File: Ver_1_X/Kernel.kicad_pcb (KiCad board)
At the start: 2 copper layers, 48.3 x 26.7 mm, 19 parts, among them J1 USB_C_Receptacle_USB2.0, J2 L, J3 R, J4 TTL, J5 Conn_01x01_Male, SW1 MODE, SW2 Reset, SW3 RePair, U1 ESP-12S-RF_Module, U2 CH340C, U3 AMS1117-3.3

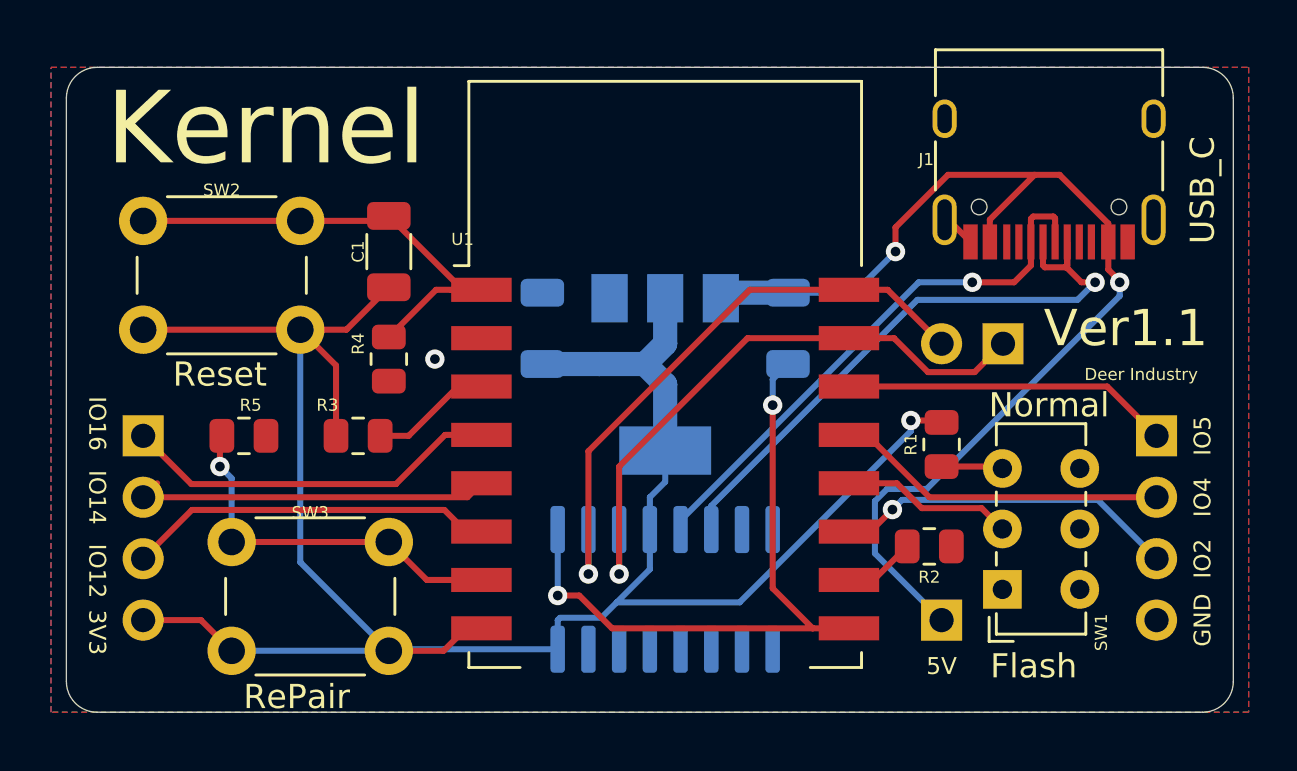
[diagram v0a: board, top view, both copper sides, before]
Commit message: fixed reset
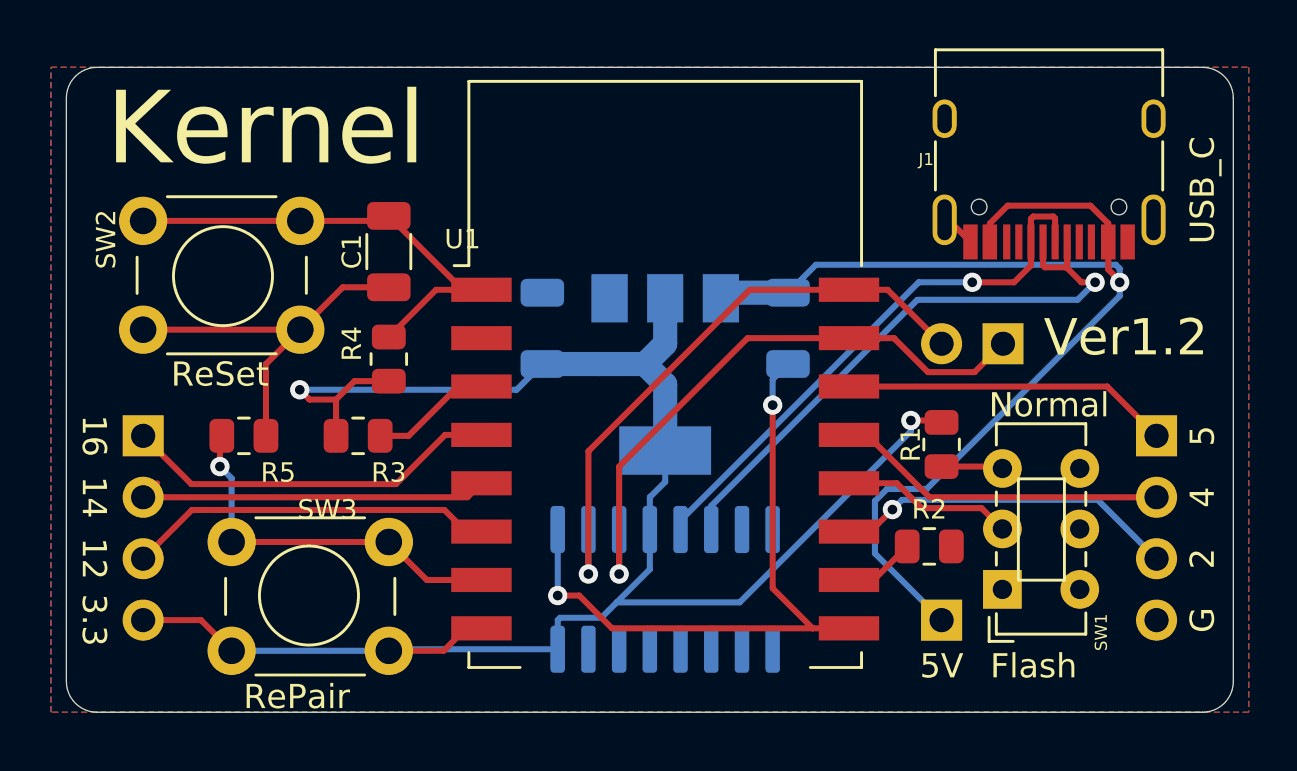
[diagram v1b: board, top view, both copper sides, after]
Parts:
- SW2: value Reset -> ReSet
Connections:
- C1 pad 1: +3V3 -> GND
- R4 pad 2: GND -> +3V3
- SW2 pad 2: +3V3 -> GND
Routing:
- net GND: track 29.6 -> 45.5 mm, vias 3 -> 2
- net +3V3: track 91.1 -> 76.6 mm, vias 1 -> 2
- net +5V: track 46.0 -> 46.9 mm, vias 2 -> 1
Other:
- board text added: "12"
- board text added: "14"
- board text added: "16"
- board text added: "2"
- board text added: "3.3"
- board text added: "4"
- board text added: "5"
- board text added: "Apple & Espressif"
- board text added: "G"
- board text added: "Homekit with ESP"
- board text added: "Luna Deer Industry"
- board text added: "Ver1.2"
- board text removed: "3V3"
- board text removed: "Deer Industry"
- board text removed: "GND"
- board text removed: "IO12"
- board text removed: "IO14"
- board text removed: "IO16"
- board text removed: "IO2"
- board text removed: "IO4"
- board text removed: "IO5"
- board text removed: "Ver1.1"

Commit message: update README
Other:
- board text added: "3v3"
- board text removed: "3.3"
